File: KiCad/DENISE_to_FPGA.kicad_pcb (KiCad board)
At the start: 2 copper layers, 78.5 x 29.5 mm, 13 parts, among them J1 Conn_01x02, J2 Conn_01x40, U1 74LVC245A, U2 74LVC245A, U3 LM1117-3.3, U4 Denise_MB_PinHeader

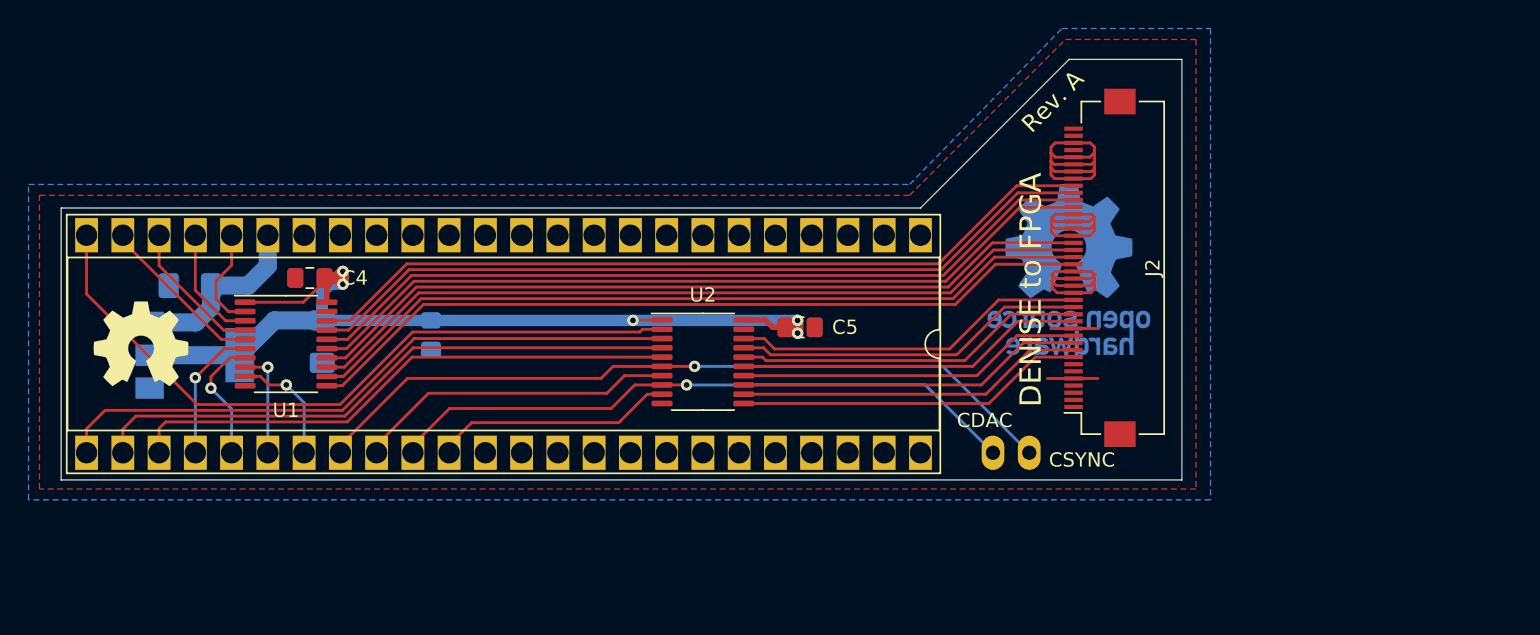
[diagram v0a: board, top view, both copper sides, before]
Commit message: Added a 74LVC1G86 XOR gate and modified the 40-pin FPC to also take a TE Connectivity 4-1734592-0, and added Hsync,Vsync-header
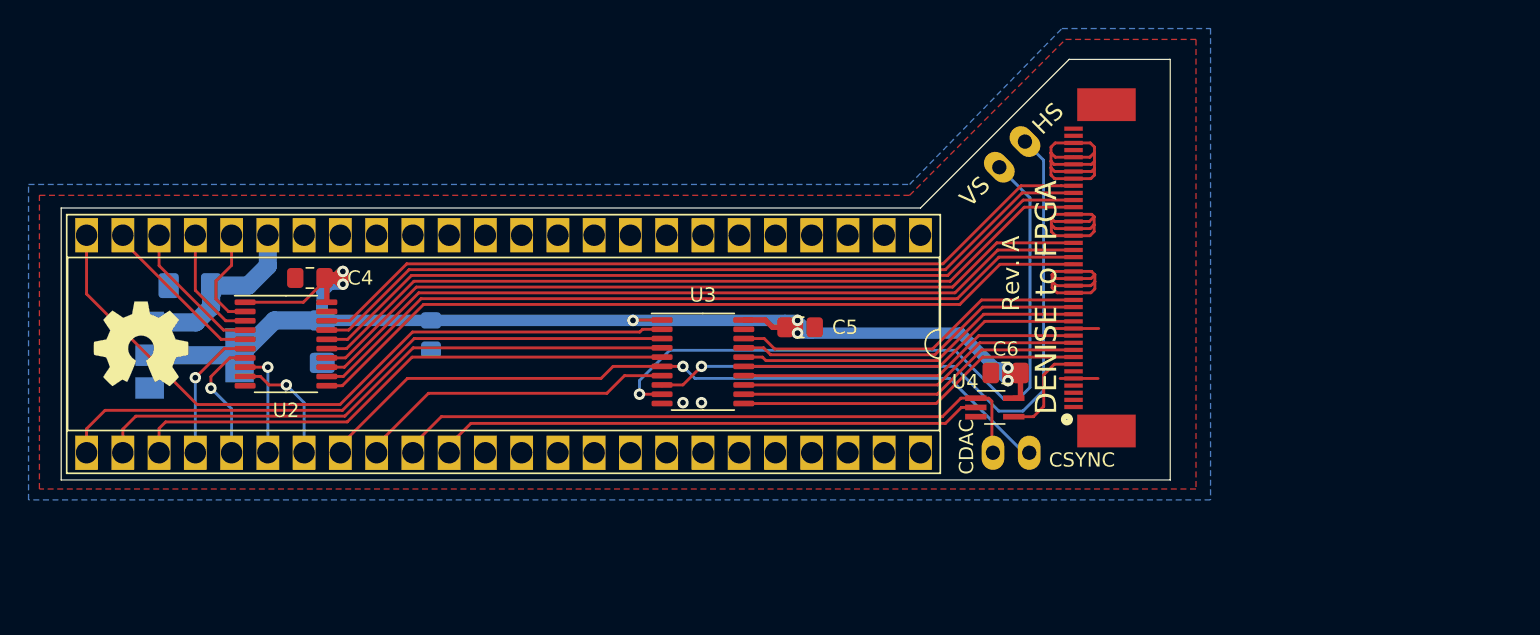
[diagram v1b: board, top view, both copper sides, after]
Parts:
- removed the REF** at (198.4, 90.6)
- added C6: 0.1uF, Capacitor_SMD:C_0805_2012Metric_Pad1.18x1.45mm_HandSolder, F.Cu at (193.9, 97.8)
- added J3: Conn_01x40, Connector_FFC-FPC:Hirose_FH12-40S-0.5SH_1x40-1MP_P0.50mm_Horizontal, F.Cu at (200.5, 90.4)
- added REF**: OSHW-Logo_11.4x12mm_SilkScreen, Symbol:OSHW-Logo_11.4x12mm_SilkScreen, B.Cu at (198.4, 90.6)
- added U4: 74LVC1G86, Package_TO_SOT_SMD:SOT-353_SC-70-5_Handsoldering, F.Cu at (193.2, 100.2)
- J2: value Conn_01x40 -> Conn_01x02; footprint Connector_FFC-FPC:Hirose_FH12-40S-0.5SH_1x40-1MP_P0.50mm_Horizontal -> Connector_PinHeader_2.54mm:PinHeader_1x02_P2.54mm_Horizontal
- moved J2 9.97 mm to (193.5, 83.4), turned to 135 degrees
- renumbered U3 to U1, U1 to U2, U2 to U3, U4 to U5
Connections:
- J2 pad 1: Net-(J2-Pad1) -> VSYNC
- J2 pad 2: Net-(J2-Pad2) -> HSYNC
- U3 pad 11: C7M_3V3 -> VSYNC_3V3
- U3 pad 12: CDAC_3V3 -> HSYNC_3V3
- U3 pad 8: CDAC -> HSYNC
- U3 pad 9: C7M -> VSYNC
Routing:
- net VSYNC: track 0.00 -> 48.9 mm, vias 0 -> 1
- net HSYNC: track 0.00 -> 47.2 mm, vias 0 -> 1
- net 3V3: track 76.4 -> 100.9 mm, vias 5 -> 7
- net VSYNC_3V3: track 0.00 -> 24.4 mm
- net C7M_3V3: track 24.4 -> 0.00 mm
- net HSYNC_3V3: track 0.00 -> 24.4 mm
- net CDAC_3V3: track 24.4 -> 0.00 mm
- net C7M: track 16.9 -> 38.5 mm
- net C14M_3V3: track 0.00 -> 7.00 mm
- net CDAC: track 45.0 -> 46.2 mm, vias 1 -> 0
- net GND: track 56.8 -> 55.7 mm, vias 0 -> 2
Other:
- board size 78.5 x 29.5 mm -> 77.7 x 29.5 mm
- board text added: "HS"
- board text added: "VS"

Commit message: Added a series resistor for C14M and changed some pin-assignments on the 40-pin FPC
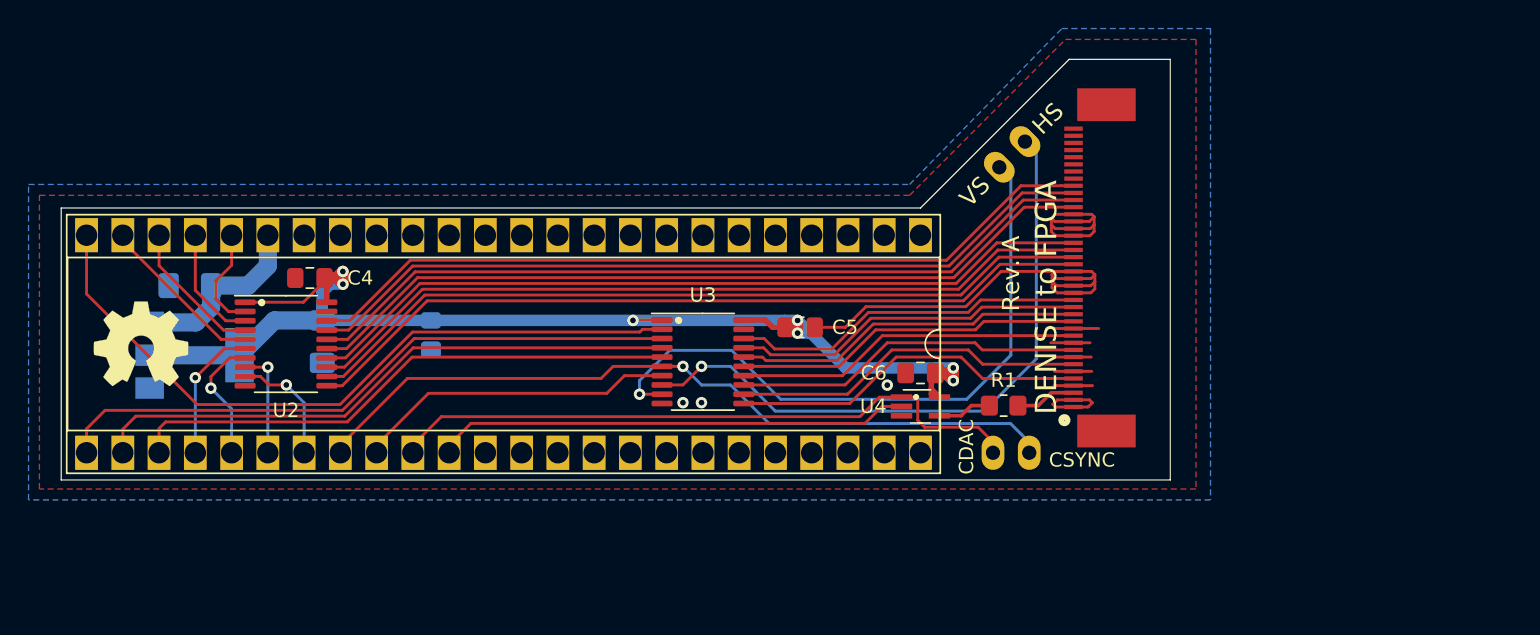
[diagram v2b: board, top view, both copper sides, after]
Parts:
- added R1: 33 Ω, Resistor_SMD:R_0805_2012Metric_Pad1.20x1.40mm_HandSolder, F.Cu at (193.8, 100.1)
- moved C6 5.97 mm to (188.0, 97.8)
- moved U4 5.21 mm to (188.0, 100.1)
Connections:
- J3 pad 1: Net-(J3-Pad1) -> GND
- J3 pad 10: PIXELSW_3V3 -> GND
- J3 pad 2: Net-(J3-Pad2) -> GND
- J3 pad 3: Net-(J3-Pad3) -> /C14M_3V3
- J3 pad 33: GND -> Net-(J3-Pad33)
- J3 pad 34: GND -> Net-(J3-Pad34)
- J3 pad 35: GND -> Net-(J3-Pad35)
- J3 pad 36: GND -> Net-(J3-Pad36)
- J3 pad 38: GND -> Net-(J3-Pad38)
- J3 pad 4: Net-(J3-Pad4) -> GND
- J3 pad 5: GND -> VSYNC_3V3
- J3 pad 6: Net-(J3-Pad6) -> GND
- J3 pad 7: C14M_3V3 -> HSYNC_3V3
- J3 pad 8: VSYNC_3V3 -> GND
- J3 pad 9: HSYNC_3V3 -> PIXELSW_3V3
- U4 pad 4: C14M_3V3 -> Net-(R1-Pad2)
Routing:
- net GND: track 55.7 -> 69.2 mm, vias 2 -> 3
- net C14M_3V3: track 7.00 -> 0.00 mm
- net C7M: track 38.5 -> 33.3 mm
- net /C14M_3V3: track 0.00 -> 4.27 mm
- net Net-(R1-Pad2): track 0.00 -> 3.79 mm
- net VSYNC: track 48.9 -> 45.6 mm
- net 3V3: track 100.9 -> 98.8 mm
- net HSYNC: track 47.2 -> 45.2 mm
- net CSYNC_3V3: track 24.3 -> 25.0 mm
- net CDAC: track 46.2 -> 45.5 mm
- net VSYNC_3V3: track 24.4 -> 25.1 mm

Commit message: changed pin assignments on the 40-pin FPC
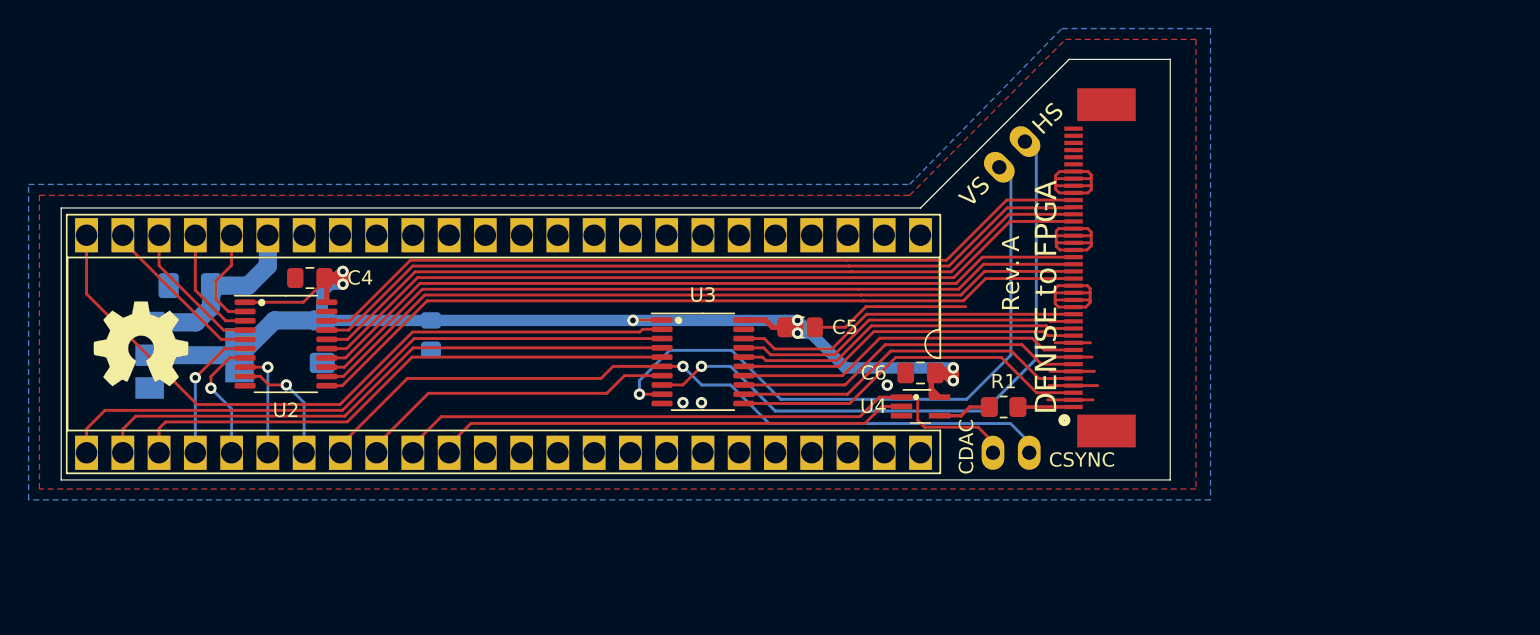
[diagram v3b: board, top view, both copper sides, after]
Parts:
- moved R1 0.10 mm to (193.8, 100.2)
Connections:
- J3 pad 1: GND -> /C14M_3V3
- J3 pad 11: CSYNC_3V3 -> B3_3V3
- J3 pad 12: GND -> B2_3V3
- J3 pad 13: B3_3V3 -> B1_3V3
- J3 pad 14: B2_3V3 -> B0_3V3
- J3 pad 15: B1_3V3 -> GND
- J3 pad 16: B0_3V3 -> GND
- J3 pad 19: GND -> G3_3V3
- J3 pad 20: GND -> G2_3V3
- J3 pad 21: G3_3V3 -> G1_3V3
- J3 pad 22: G2_3V3 -> G0_3V3
- J3 pad 23: G1_3V3 -> GND
- J3 pad 24: G0_3V3 -> GND
- J3 pad 27: GND -> R3_3V3
- J3 pad 28: GND -> R2_3V3
- J3 pad 29: R3_3V3 -> R1_3V3
- J3 pad 3: /C14M_3V3 -> VSYNC_3V3
- J3 pad 30: R2_3V3 -> R0_3V3
- J3 pad 31: R1_3V3 -> GND
- J3 pad 32: R0_3V3 -> GND
- J3 pad 33: Net-(J3-Pad33) -> GND
- J3 pad 34: Net-(J3-Pad34) -> GND
- J3 pad 5: VSYNC_3V3 -> HSYNC_3V3
- J3 pad 7: HSYNC_3V3 -> PIXELSW_3V3
- J3 pad 9: PIXELSW_3V3 -> CSYNC_3V3
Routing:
- net GND: track 69.2 -> 63.3 mm

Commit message: Removed unused nets, added no-connect flags
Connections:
- net BURST renamed Net-(U5-Pad18)
- net CCK renamed Net-(U5-Pad36)
- net D0 renamed Net-(U5-Pad7)
- net D1 renamed Net-(U5-Pad6)
- net D10 renamed Net-(U5-Pad45)
- net D11 renamed Net-(U5-Pad44)
- net D12 renamed Net-(U5-Pad43)
- net D13 renamed Net-(U5-Pad42)
- net D14 renamed Net-(U5-Pad41)
- net D15 renamed Net-(U5-Pad40)
- net D2 renamed Net-(U5-Pad5)
- net D3 renamed Net-(U5-Pad4)
- net D4 renamed Net-(U5-Pad3)
- net D5 renamed Net-(U5-Pad2)
- net D6 renamed Net-(U5-Pad1)
- net D7 renamed Net-(U5-Pad48)
- net D8 renamed Net-(U5-Pad47)
- net D9 renamed Net-(U5-Pad46)
- net M0H renamed Net-(U5-Pad9)
- net M0V renamed Net-(U5-Pad38)
- net M1H renamed Net-(U5-Pad8)
- net M1V renamed Net-(U5-Pad39)
- net RGA1 renamed Net-(U5-Pad17)
- net RGA2 renamed Net-(U5-Pad16)
- net RGA3 renamed Net-(U5-Pad15)
- net RGA4 renamed Net-(U5-Pad14)
- net RGA5 renamed Net-(U5-Pad13)
- net RGA6 renamed Net-(U5-Pad12)
- net RGA7 renamed Net-(U5-Pad11)
- net RGA8 renamed Net-(U5-Pad10)

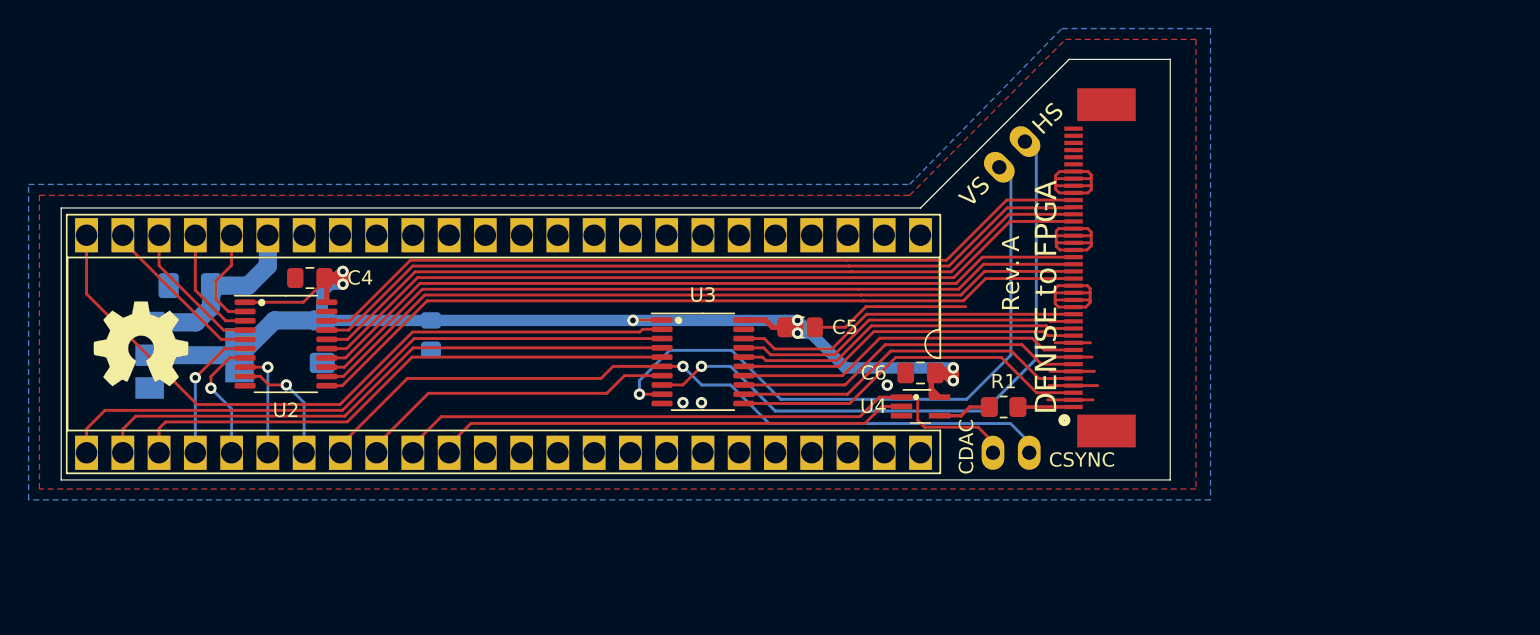
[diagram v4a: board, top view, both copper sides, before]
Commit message: small adjustment of board length
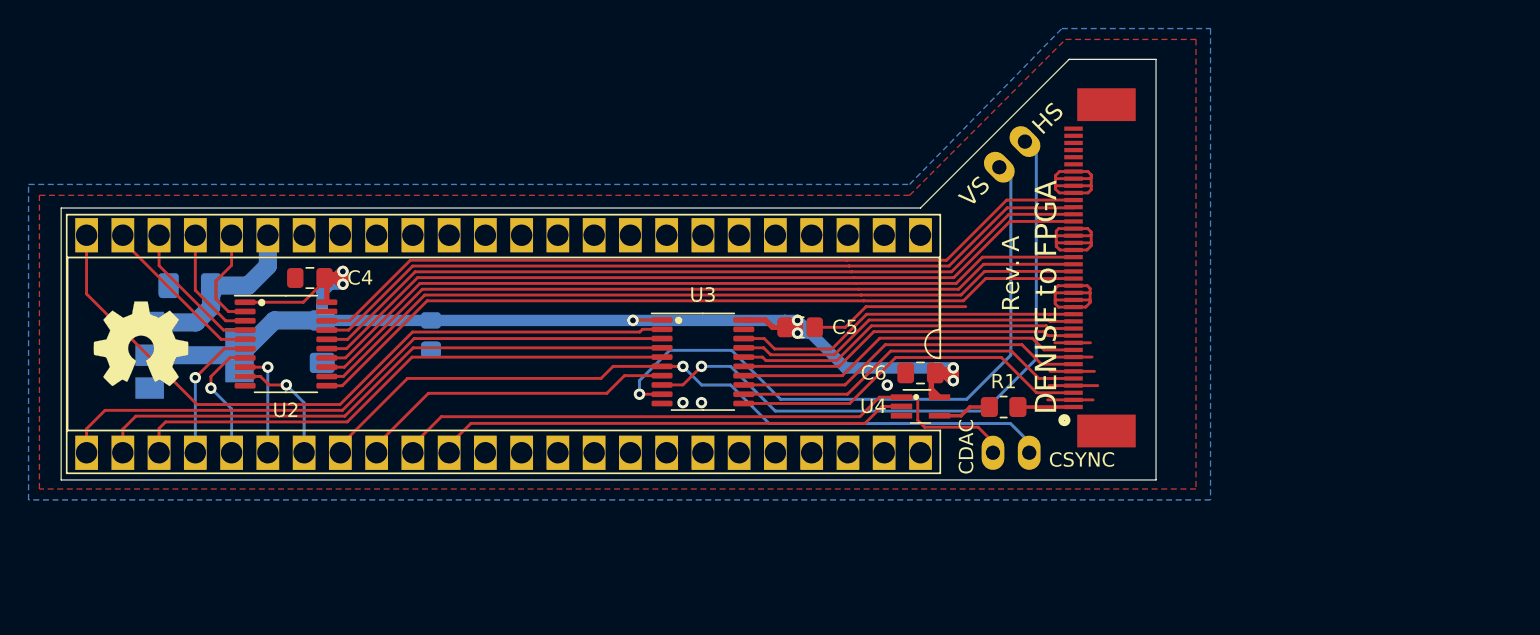
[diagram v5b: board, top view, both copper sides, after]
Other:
- board size 77.7 x 29.5 mm -> 76.7 x 29.5 mm

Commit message: small silkscreen fix
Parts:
- moved REF** 1.76 mm to (196.8, 91.2)
